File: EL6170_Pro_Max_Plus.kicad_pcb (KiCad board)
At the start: 2 copper layers, 128 x 70 mm, 0 parts

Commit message: key
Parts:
- added C1: 0.1uF, SparkFun-Capacitor:C_0603_1608Metric, F.Cu at (360.9, 159.2)
- added C10: 1uF, SparkFun-Capacitor:C_0402_1005Metric, F.Cu at (380.4, 162.9)
- added C11: 10uF, SparkFun-Capacitor:C_0402_1005Metric, F.Cu at (380.4, 164.8)
- added C12: 0.1uF, SparkFun-Capacitor:C_0402_1005Metric, F.Cu at (380.4, 166.8)
- added C13: 0.1uF, SparkFun-Capacitor:C_0402_1005Metric, F.Cu at (380.4, 168.8)
- added C14: 0.1uF, SparkFun-Capacitor:C_0402_1005Metric, F.Cu at (380.4, 170.7)
- added C15: 0.1uF, SparkFun-Capacitor:C_0402_1005Metric, F.Cu at (383.2, 158.9)
- added C16: 10uF, SparkFun-Capacitor:C_0402_1005Metric, F.Cu at (383.2, 160.9)
- added C17: 0.1uF, SparkFun-Capacitor:C_0402_1005Metric, F.Cu at (383.2, 162.9)
- added C18: 10uF, SparkFun-Capacitor:C_0402_1005Metric, F.Cu at (383.2, 164.8)
- added C19: 0.1uF, SparkFun-Capacitor:C_0402_1005Metric, F.Cu at (383.2, 166.8)
- added C2: 4.7uF, SparkFun-Capacitor:C_0603_1608Metric, F.Cu at (360.9, 161.7)
- added C20: 1uF, SparkFun-Capacitor:C_0402_1005Metric, F.Cu at (383.2, 168.8)
- added C21: 0.1uF, SparkFun-Capacitor:C_0402_1005Metric, F.Cu at (383.2, 170.7)
- added C22: 10pF, SparkFun-Capacitor:C_0603_1608Metric, F.Cu at (360.9, 176.8)
- added C23: 10pF, SparkFun-Capacitor:C_0603_1608Metric, F.Cu at (360.9, 179.3)
- added C24: 10uF, SparkFun-Capacitor:C_0402_1005Metric, F.Cu at (386.1, 158.9)
- added C25: 0.1uF, SparkFun-Capacitor:C_0402_1005Metric, F.Cu at (386.1, 160.9)
- added C26: 4.7pF, SparkFun-Capacitor:C_0402_1005Metric, F.Cu at (386.1, 162.9)
- added C27: 2.2nF, SparkFun-Capacitor:C_0603_1608Metric, F.Cu at (364.9, 159.2)
- added C28: 2.2nF, SparkFun-Capacitor:C_0603_1608Metric, F.Cu at (364.9, 161.7)
- added C29: 2.2uF, SparkFun-Capacitor:C_0603_1608Metric, F.Cu at (364.9, 164.2)
- added C3: 0.1uF, SparkFun-Capacitor:C_0603_1608Metric, F.Cu at (360.9, 164.2)
- added C30: 2.2uF, SparkFun-Capacitor:C_0603_1608Metric, F.Cu at (364.9, 166.7)
- added C31: 0.1uF, SparkFun-Capacitor:C_0603_1608Metric, F.Cu at (364.9, 169.2)
- added C32: 0.1uF, SparkFun-Capacitor:C_0603_1608Metric, F.Cu at (364.9, 171.7)
- added C33: 0.1uF, SparkFun-Capacitor:C_0603_1608Metric, F.Cu at (364.9, 174.3)
- added C34: 0.1uF, SparkFun-Capacitor:C_0603_1608Metric, F.Cu at (364.9, 176.8)
- added C35: 10uF, SparkFun-Capacitor:C_0603_1608Metric, F.Cu at (364.9, 179.3)
- added C36: 1uF, SparkFun-Capacitor:C_0603_1608Metric, F.Cu at (368.9, 159.2)
- added C37: 1uF, SparkFun-Capacitor:C_0603_1608Metric, F.Cu at (368.9, 161.7)
- added C38: 0.1uF, SparkFun-Capacitor:C_0603_1608Metric, F.Cu at (368.9, 164.2)
- added C39: 47uF, SparkFun-Capacitor:C_0805_2012Metric, F.Cu at (388.9, 153.3)
- added C4: 4.7uF, SparkFun-Capacitor:C_0603_1608Metric, F.Cu at (360.9, 166.7)
- added C40: 22uF, SparkFun-Capacitor:C_0603_1608Metric, F.Cu at (368.9, 166.7)
- added C41: 22uF, SparkFun-Capacitor:C_0603_1608Metric, F.Cu at (368.9, 169.2)
- added C42: 0.1uF, SparkFun-Capacitor:C_0603_1608Metric, F.Cu at (368.9, 171.7)
- added C43: 10uF, SparkFun-Capacitor:C_0603_1608Metric, F.Cu at (368.9, 174.3)
- added C44: 10uF, SparkFun-Capacitor:C_0402_1005Metric, F.Cu at (386.1, 164.8)
- added C45: 0.1uF, SparkFun-Capacitor:C_0402_1005Metric, F.Cu at (386.1, 166.8)
- added C5: 4.7uF, SparkFun-Capacitor:C_0603_1608Metric, F.Cu at (360.9, 169.2)
- added C6: 4.7uF, SparkFun-Capacitor:C_0603_1608Metric, F.Cu at (360.9, 171.7)
- added C7: 4.7uF, SparkFun-Capacitor:C_0603_1608Metric, F.Cu at (360.9, 174.3)
- added C8: 8.2pF, Capacitor_SMD:C_0402_1005Metric, F.Cu at (380.4, 158.9)
- added C9: 0.1uF, SparkFun-Capacitor:C_0402_1005Metric, F.Cu at (380.4, 160.9)
- added CN1: PJ-327A0-SMT, easyeda2kicad:AUDIO-SMD_PJ-327A0-SMT, F.Cu at (385.8, 138.5)
- added D1: LED, SparkFun-LED:LED_0603_1608Metric, F.Cu at (368.9, 176.8)
- added D10: LESD8D3.3CAT5G, Diode_SMD:D_SOD-882, F.Cu at (394.6, 191.1)
- added D11: LESD8D3.3CAT5G, Diode_SMD:D_SOD-882, F.Cu at (394.6, 193.4)
- added D12: 1N4148WS, Diode_SMD:D_SOD-323, F.Cu at (308.1, 159.4)
- added D13: 1N4148WS, Diode_SMD:D_SOD-323, F.Cu at (308.1, 162.4)
- added D14: 1N4148WS, Diode_SMD:D_SOD-323, F.Cu at (308.1, 165.3)
- added D15: 1N4148WS, Diode_SMD:D_SOD-323, F.Cu at (308.1, 168.3)
- added D16: 1N4148WS, Diode_SMD:D_SOD-323, F.Cu at (308.1, 171.2)
- added D17: 1N4148WS, Diode_SMD:D_SOD-323, F.Cu at (308.1, 174.2)
- added D18: 1N4148WS, Diode_SMD:D_SOD-323, F.Cu at (308.1, 177.1)
- added D19: 1N4148WS, Diode_SMD:D_SOD-323, F.Cu at (308.1, 180.1)
- added D2: LED, SparkFun-LED:LED_0603_1608Metric, F.Cu at (368.9, 179.3)
- added D20: 1N4148WS, Diode_SMD:D_SOD-323, F.Cu at (308.1, 183.0)
- added D21: 1N4148WS, Diode_SMD:D_SOD-323, F.Cu at (312.4, 159.4)
- added D22: 1N4148WS, Diode_SMD:D_SOD-323, F.Cu at (312.4, 162.4)
- added D23: 1N4148WS, Diode_SMD:D_SOD-323, F.Cu at (312.4, 165.3)
- added D24: 1N4148WS, Diode_SMD:D_SOD-323, F.Cu at (312.4, 168.3)
- added D25: 1N4148WS, Diode_SMD:D_SOD-323, F.Cu at (312.4, 171.2)
- added D26: 1N4148WS, Diode_SMD:D_SOD-323, F.Cu at (312.4, 174.2)
- added D27: 1N4148WS, Diode_SMD:D_SOD-323, F.Cu at (312.4, 177.1)
- added D28: 1N4148WS, Diode_SMD:D_SOD-323, F.Cu at (312.4, 180.1)
- added D29: 1N4148WS, Diode_SMD:D_SOD-323, F.Cu at (312.4, 183.0)
- added D3: SS14, Diode_SMD:D_SMA, F.Cu at (324.4, 193.3)
- added D30: 1N4148WS, Diode_SMD:D_SOD-323, F.Cu at (316.7, 159.4)
- added D31: 1N4148WS, Diode_SMD:D_SOD-323, F.Cu at (316.7, 162.4)
- added D32: 1N4148WS, Diode_SMD:D_SOD-323, F.Cu at (316.7, 165.3)
- added D33: 1N4148WS, Diode_SMD:D_SOD-323, F.Cu at (316.7, 168.3)
- added D34: 1N4148WS, Diode_SMD:D_SOD-323, F.Cu at (316.7, 171.2)
- added D35: 1N4148WS, Diode_SMD:D_SOD-323, F.Cu at (316.7, 174.2)
- added D36: 1N4148WS, Diode_SMD:D_SOD-323, F.Cu at (316.7, 177.1)
- added D37: 1N4148WS, Diode_SMD:D_SOD-323, F.Cu at (316.7, 180.1)
- added D38: 1N4148WS, Diode_SMD:D_SOD-323, F.Cu at (316.7, 183.0)
- added D39: 1N4148WS, Diode_SMD:D_SOD-323, F.Cu at (321.0, 159.4)
- added D4: LED, SparkFun-LED:LED_0603_1608Metric, F.Cu at (372.9, 159.2)
- added D40: 1N4148WS, Diode_SMD:D_SOD-323, F.Cu at (321.0, 162.4)
- added D41: 1N4148WS, Diode_SMD:D_SOD-323, F.Cu at (321.0, 165.3)
- added D42: 1N4148WS, Diode_SMD:D_SOD-323, F.Cu at (321.0, 168.3)
- added D43: 1N4148WS, Diode_SMD:D_SOD-323, F.Cu at (321.0, 171.2)
- added D44: 1N4148WS, Diode_SMD:D_SOD-323, F.Cu at (321.0, 174.2)
- added D45: 1N4148WS, Diode_SMD:D_SOD-323, F.Cu at (321.0, 177.1)
- added D46: 1N4148WS, Diode_SMD:D_SOD-323, F.Cu at (321.0, 180.1)
- added D47: 1N4148WS, Diode_SMD:D_SOD-323, F.Cu at (321.0, 183.0)
- added D48: 1N4148WS, Diode_SMD:D_SOD-323, F.Cu at (325.3, 159.4)
- added D49: 1N4148WS, Diode_SMD:D_SOD-323, F.Cu at (325.3, 162.4)
- added D5: SS34, Diode_SMD:D_SMA, F.Cu at (324.4, 197.9)
- added D50: 1N4148WS, Diode_SMD:D_SOD-323, F.Cu at (325.3, 165.3)
- added D51: 1N4148WS, Diode_SMD:D_SOD-323, F.Cu at (325.3, 168.3)
- added D52: 1N4148WS, Diode_SMD:D_SOD-323, F.Cu at (325.3, 171.2)
- added D53: 1N4148WS, Diode_SMD:D_SOD-323, F.Cu at (325.3, 174.2)
- added D54: 1N4148WS, Diode_SMD:D_SOD-323, F.Cu at (325.3, 177.1)
- added D55: 1N4148WS, Diode_SMD:D_SOD-323, F.Cu at (325.3, 180.1)
- added D56: 1N4148WS, Diode_SMD:D_SOD-323, F.Cu at (325.3, 183.0)
- added D57: 1N4148WS, Diode_SMD:D_SOD-323, F.Cu at (329.6, 159.4)
- added D58: 1N4148WS, Diode_SMD:D_SOD-323, F.Cu at (329.6, 162.4)
- added D59: 1N4148WS, Diode_SMD:D_SOD-323, F.Cu at (329.6, 165.3)
- added D6: LESD8D3.3CAT5G, Diode_SMD:D_SOD-882, F.Cu at (394.6, 181.7)
- added D60: 1N4148WS, Diode_SMD:D_SOD-323, F.Cu at (329.6, 168.3)
- added D61: 1N4148WS, Diode_SMD:D_SOD-323, F.Cu at (329.6, 171.2)
- added D62: 1N4148WS, Diode_SMD:D_SOD-323, F.Cu at (329.6, 174.2)
- added D63: 1N4148WS, Diode_SMD:D_SOD-323, F.Cu at (329.6, 177.1)
- added D64: 1N4148WS, Diode_SMD:D_SOD-323, F.Cu at (329.6, 180.1)
- added D7: LESD8D3.3CAT5G, Diode_SMD:D_SOD-882, F.Cu at (394.6, 184.0)
- added D8: LESD8D3.3CAT5G, Diode_SMD:D_SOD-882, F.Cu at (394.6, 186.4)
- added D9: LESD8D3.3CAT5G, Diode_SMD:D_SOD-882, F.Cu at (394.6, 188.7)
- added J1: USB_C_Receptacle, SparkFun-Connector:USB-C_16, F.Cu at (387.1, 122.0)
- added J2: microSD, SparkFun-Connector:microSD_External_Pin, F.Cu at (340.8, 170.0)
- added L1: 39nH, Inductor_SMD:L_0402_1005Metric, F.Cu at (383.1, 110.3)
- added L2: 1.3nH, Inductor_SMD:L_0402_1005Metric, F.Cu at (383.1, 112.3)
- added L3: 2nH, Inductor_SMD:L_0402_1005Metric, F.Cu at (383.1, 114.3)
- added L4: 2nH, Inductor_SMD:L_0402_1005Metric, F.Cu at (383.1, 116.3)
- added L5: 10uH_5x5mm_1.0A, SparkFun-Coil:Inductor_4.7x4.7mm, F.Cu at (390.9, 161.3)
- added L6: SCCD43-220KT, easyeda2kicad:IND-SMD_L4.5-W4.0_SCCD43, F.Cu at (390.9, 167.6)
- added Q1: MMBT3904, Package_TO_SOT_SMD:SOT-23, F.Cu at (379.2, 111.7)
- added Q2: MMBT3904, Package_TO_SOT_SMD:SOT-23, F.Cu at (379.2, 116.4)
- added Q3: 2N7002, Package_TO_SOT_SMD:SOT-23, F.Cu at (379.2, 121.0)
- added Q4: AO3401A, Package_TO_SOT_SMD:SOT-23, F.Cu at (379.2, 125.6)
- added Q5: AO3401A, Package_TO_SOT_SMD:SOT-23, F.Cu at (379.2, 130.2)
- added R1: 560, SparkFun-Resistor:R_0402_1005Metric, F.Cu at (383.1, 118.3)
- added R10: 15k, SparkFun-Resistor:R_0603_1608Metric, F.Cu at (372.9, 161.7)
- added R11: 205K, SparkFun-Resistor:R_0603_1608Metric, F.Cu at (372.9, 164.2)
- added R12: 1.8M, SparkFun-Resistor:R_0603_1608Metric, F.Cu at (372.9, 166.7)
- added R13: 470, SparkFun-Resistor:R_0603_1608Metric, F.Cu at (372.9, 169.2)
- added R14: 470, SparkFun-Resistor:R_0603_1608Metric, F.Cu at (372.9, 171.7)
- added R15: 470, SparkFun-Resistor:R_0603_1608Metric, F.Cu at (372.9, 174.3)
- added R16: 470, SparkFun-Resistor:R_0603_1608Metric, F.Cu at (372.9, 176.8)
- added R17: 470, SparkFun-Resistor:R_0603_1608Metric, F.Cu at (372.9, 179.3)
- added R18: 470, SparkFun-Resistor:R_0603_1608Metric, F.Cu at (376.9, 159.2)
- added R19: 0, SparkFun-Resistor:R_0603_1608Metric, F.Cu at (376.9, 161.7)
- added R2: 5.1k, SparkFun-Resistor:R_0402_1005Metric, F.Cu at (383.1, 120.3)
- added R20: 1k, SparkFun-Resistor:R_0603_1608Metric, F.Cu at (376.9, 164.2)
- added R21: 330, SparkFun-Resistor:R_0603_1608Metric, F.Cu at (376.9, 166.7)
- added R22: 330, SparkFun-Resistor:R_0603_1608Metric, F.Cu at (376.9, 169.2)
- added R23: 2, SparkFun-Resistor:R_0603_1608Metric, F.Cu at (376.9, 171.7)
- added R24: 10k, SparkFun-Resistor:R_0402_1005Metric, F.Cu at (388.9, 112.3)
- added R25: 10k, SparkFun-Resistor:R_0402_1005Metric, F.Cu at (388.9, 114.3)
- added R26: 10k, SparkFun-Resistor:R_0402_1005Metric, F.Cu at (388.9, 116.3)
- added R27: 10k, SparkFun-Resistor:R_0402_1005Metric, F.Cu at (388.9, 118.3)
- added R28: 10k, SparkFun-Resistor:R_0402_1005Metric, F.Cu at (388.9, 120.3)
- added R29: 10k, SparkFun-Resistor:R_0402_1005Metric, F.Cu at (391.8, 110.3)
- added R3: 5.1k, SparkFun-Resistor:R_0402_1005Metric, F.Cu at (386.0, 110.3)
- added R30: 10k, SparkFun-Resistor:R_0402_1005Metric, F.Cu at (391.8, 112.3)
- added R31: 10k, SparkFun-Resistor:R_0402_1005Metric, F.Cu at (391.8, 114.3)
- added R32: 10k, SparkFun-Resistor:R_0402_1005Metric, F.Cu at (391.8, 116.3)
- added R33: 10k, SparkFun-Resistor:R_0402_1005Metric, F.Cu at (391.8, 118.3)
- added R4: 4.7k, SparkFun-Resistor:R_0402_1005Metric, F.Cu at (386.0, 112.3)
- added R5: 4.7k, SparkFun-Resistor:R_0402_1005Metric, F.Cu at (386.0, 114.3)
- added R6: 4.7k, SparkFun-Resistor:R_0402_1005Metric, F.Cu at (386.0, 116.3)
- added R7: 499, SparkFun-Resistor:R_0402_1005Metric, F.Cu at (386.0, 118.3)
- added R8: 4.7k, SparkFun-Resistor:R_0402_1005Metric, F.Cu at (386.0, 120.3)
- added R9: 4.7k, SparkFun-Resistor:R_0402_1005Metric, F.Cu at (388.9, 110.3)
- added SH1: ~, SH1122:SH1122_FPC, F.Cu at (386.1, 151.1)
- added SW1: SW_LEFT, Butm:MaskBtm6mmBh, B.Cu at (147.5, 76.5)
- added SW10: SW_K4, Butm:MaskBtm4mmBh, B.Cu at (175.0, 90.5)
- added SW11: SW_K5, Butm:MaskBtm4mmBh, B.Cu at (162.5, 90.5)
- added SW12: SW_K6, Butm:MaskBtm4mmBh, B.Cu at (150.0, 90.5)
- added SW13: SW_K7, Butm:MaskBtm4mmBh, B.Cu at (137.5, 90.5)
- added SW14: SW_K8, Butm:MaskBtm4mmBh, B.Cu at (125.0, 90.5)
- added SW15: SW_K9, Butm:MaskBtm4mmBh, B.Cu at (112.5, 90.5)
- added SW16: SW_K0, Butm:MaskBtm4mmBh, B.Cu at (100.0, 90.5)
- added SW17: SW_KQ, Butm:MaskBtm5mm, B.Cu at (163.3, 146.1)
- added SW18: SW_KW, Butm:MaskBtm5mm, B.Cu at (163.3, 154.2)
- added SW19: SW_KE, Butm:MaskBtm5mm, B.Cu at (163.3, 162.3)
- added SW2: SW_UP, Butm:MaskBtm6mm, B.Cu at (136.5, 71.5)
- added SW20: SW_KR, Butm:MaskBtm5mm, B.Cu at (163.3, 170.4)
- added SW21: SW_KT, Butm:MaskBtm5mm, B.Cu at (163.3, 178.5)
- added SW22: SW_KY, Butm:MaskBtm5mm, B.Cu at (163.3, 186.6)
- added SW23: SW_KU, Butm:MaskBtm5mm, B.Cu at (155.2, 146.1)
- added SW24: SW_KI, Butm:MaskBtm5mm, B.Cu at (155.2, 154.2)
- added SW25: SW_KO, Butm:MaskBtm5mm, B.Cu at (155.2, 162.3)
- added SW26: SW_KP, Butm:MaskBtm5mm, B.Cu at (155.2, 170.4)
- added SW27: SW_KA, Butm:MaskBtm5mm, B.Cu at (155.2, 178.5)
- added SW28: SW_KS, Butm:MaskBtm5mm, B.Cu at (155.2, 186.6)
- added SW29: SW_KD, Butm:MaskBtm5mm, B.Cu at (147.1, 146.1)
- added SW3: SW_DOWN, Butm:MaskBtm6mm, B.Cu at (136.5, 81.0)
- added SW30: SW_KF, Butm:MaskBtm5mm, B.Cu at (147.1, 154.2)
- added SW31: SW_KG, Butm:MaskBtm5mm, B.Cu at (147.1, 162.3)
- added SW32: SW_KH, Butm:MaskBtm5mm, B.Cu at (147.1, 170.4)
- added SW33: SW_KJ, Butm:MaskBtm5mm, B.Cu at (147.1, 178.5)
- added SW34: SW_KK, Butm:MaskBtm5mm, B.Cu at (147.1, 186.6)
- added SW35: SW_KL, Butm:MaskBtm5mm, B.Cu at (139.0, 146.1)
- added SW36: SW_KZ, Butm:MaskBtm5mm, B.Cu at (139.0, 154.2)
- added SW37: SW_KX, Butm:MaskBtm5mm, B.Cu at (139.0, 162.3)
- added SW38: SW_KC, Butm:MaskBtm5mm, B.Cu at (139.0, 170.4)
- added SW39: SW_KV, Butm:MaskBtm5mm, B.Cu at (139.0, 178.5)
- added SW4: SW_RIGHT, Butm:MaskBtm6mmBh, B.Cu at (125.5, 76.5)
- added SW40: SW_KB, Butm:MaskBtm5mm, B.Cu at (139.0, 186.6)
- added SW41: SW_KN, Butm:MaskBtm5mm, B.Cu at (130.9, 146.1)
- added SW42: SW_KM, Butm:MaskBtm5mm, B.Cu at (130.9, 154.2)
- added SW43: SW_KCOM, Butm:MaskBtm5mm, B.Cu at (130.9, 162.3)
- added SW44: SW_KDOT, Butm:MaskBtm5mm, B.Cu at (130.9, 170.4)
- added SW45: SW_SHIFT, Butm:MaskBtm5mm, B.Cu at (130.9, 178.5)
- added SW46: SW_CE(IO0), Butm:MaskBtm5mm, B.Cu at (130.9, 186.6)
- added SW47: SW_OFF, Butm:MaskBtm5mm, B.Cu at (122.8, 146.1)
- added SW48: SW_SECRET, Butm:MaskBtm5mm, B.Cu at (122.8, 154.2)
- added SW49: SW_MCK, Butm:MaskBtm5mm, B.Cu at (122.8, 162.3)
- added SW5: SW_UP2, Butm:MaskBtm6mm, B.Cu at (113.0, 76.5)
- added SW50: SW_SPACE, Butm:MaskBtm5mmBh, B.Cu at (200.9, 170.3)
- added SW51: SW_REMARK, Butm:MaskBtm5mm, B.Cu at (122.8, 170.4)
- added SW52: SW_CALENDAR, Butm:MaskBtm5mm, B.Cu at (122.8, 178.5)
- added SW53: SW_MODE, Butm:MaskBtm5mm, B.Cu at (122.8, 186.6)
- added SW54: SW_ENTER, Butm:MaskBtm5mmBh, B.Cu at (199.0, 186.3)
- added SW6: SW_DOWN2, Butm:MaskBtm6mm, B.Cu at (100.5, 76.5)
- added SW7: SW_K1, Butm:MaskBtm4mmBh, B.Cu at (212.5, 90.5)
- added SW8: SW_K2, Butm:MaskBtm4mmBh, B.Cu at (200.0, 90.5)
- added SW9: SW_K3, Butm:MaskBtm4mmBh, B.Cu at (187.5, 90.5)
- added SWBOOT1: BOOT, Butm:MaskBtm4mm, F.Cu at (335.3, 190.5)
- added SWRST1: RST, Butm:MaskBtm4mm, F.Cu at (335.3, 197.6)
- added U1: ESP32-S3, Package_DFN_QFN:QFN-56-1EP_7x7mm_P0.4mm_EP4x4mm, F.Cu at (315.7, 189.1)
- added U10: ME6211C33M5, Package_TO_SOT_SMD:SOT-23-5, F.Cu at (308.5, 196.1)
- added U11: TP5400_C2891434, easyeda2kicad:ESOP-8_L4.9-W3.9-P1.27-LS6.0-BL-EP, F.Cu at (391.9, 175.7)
- added U12: PCF8575DBR, Package_SO:SSOP-24_5.3x8.2mm_P0.65mm, F.Cu at (344.1, 192.0)
- added U2: TPS61040DBV, Package_TO_SOT_SMD:SOT-23-5, F.Cu at (308.5, 186.9)
- added U3: ESP-PSRAM64H, Package_SO:SOIC-8_3.9x4.9mm_P1.27mm, F.Cu at (354.0, 197.7)
- added U4: W25Q128JVS, Package_SO:SOIC-8_5.23x5.23mm_P1.27mm, F.Cu at (359.7, 150.5)
- added U5: ME6217C33M5, Package_TO_SOT_SMD:SOT-23-5, F.Cu at (308.5, 191.5)
- added U6: CH340K, Package_SO:SSOP-10-1EP_3.9x4.9mm_P1mm_EP2.1x3.3mm, F.Cu at (315.4, 197.2)
- added U7: RFANT5220110A0T, easyeda2kicad:FILTER-SMD_L5.2-W2.0-L, F.Cu at (325.8, 187.8)
- added U8: CH334R, Package_SO:QSOP-16_3.9x4.9mm_P0.635mm, F.Cu at (369.5, 150.3)
- added U9: PCM5102A, Package_SO:TSSOP-20_4.4x6.5mm_P0.65mm, F.Cu at (383.7, 175.8)
- added X1: 40MHz, easyeda2kicad:CRYSTAL-SMD_4P-L2.5-W2.0-BL, F.Cu at (379.3, 153.9)
- added X2: 12MHz, easyeda2kicad:CRYSTAL-SMD_4P-L2.5-W2.0-BL-A, F.Cu at (384.3, 153.9)

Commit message: sync
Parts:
- moved C24 318.5 mm to (67.8, 145.7)
- moved C25 318.5 mm to (67.8, 147.6)
- moved C26 318.5 mm to (67.8, 149.6)
- moved C44 318.5 mm to (67.8, 151.6)
- moved C45 318.5 mm to (67.8, 153.5)
- moved D21 318.5 mm to (-5.84, 146.1)
- moved D22 318.5 mm to (-5.84, 149.1)
- moved D23 318.5 mm to (-5.84, 152.0)
- moved D24 318.5 mm to (-5.84, 155.0)
- moved D25 318.5 mm to (-5.84, 157.9)
- moved D26 318.5 mm to (-5.84, 160.9)
- moved D27 318.5 mm to (-5.84, 163.8)
- moved D28 318.5 mm to (-5.84, 166.8)
- moved D29 318.5 mm to (-5.84, 169.7)
- moved D30 318.5 mm to (-1.55, 146.1)
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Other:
- board size 128 x 70 mm -> 128 x 70.5 mm

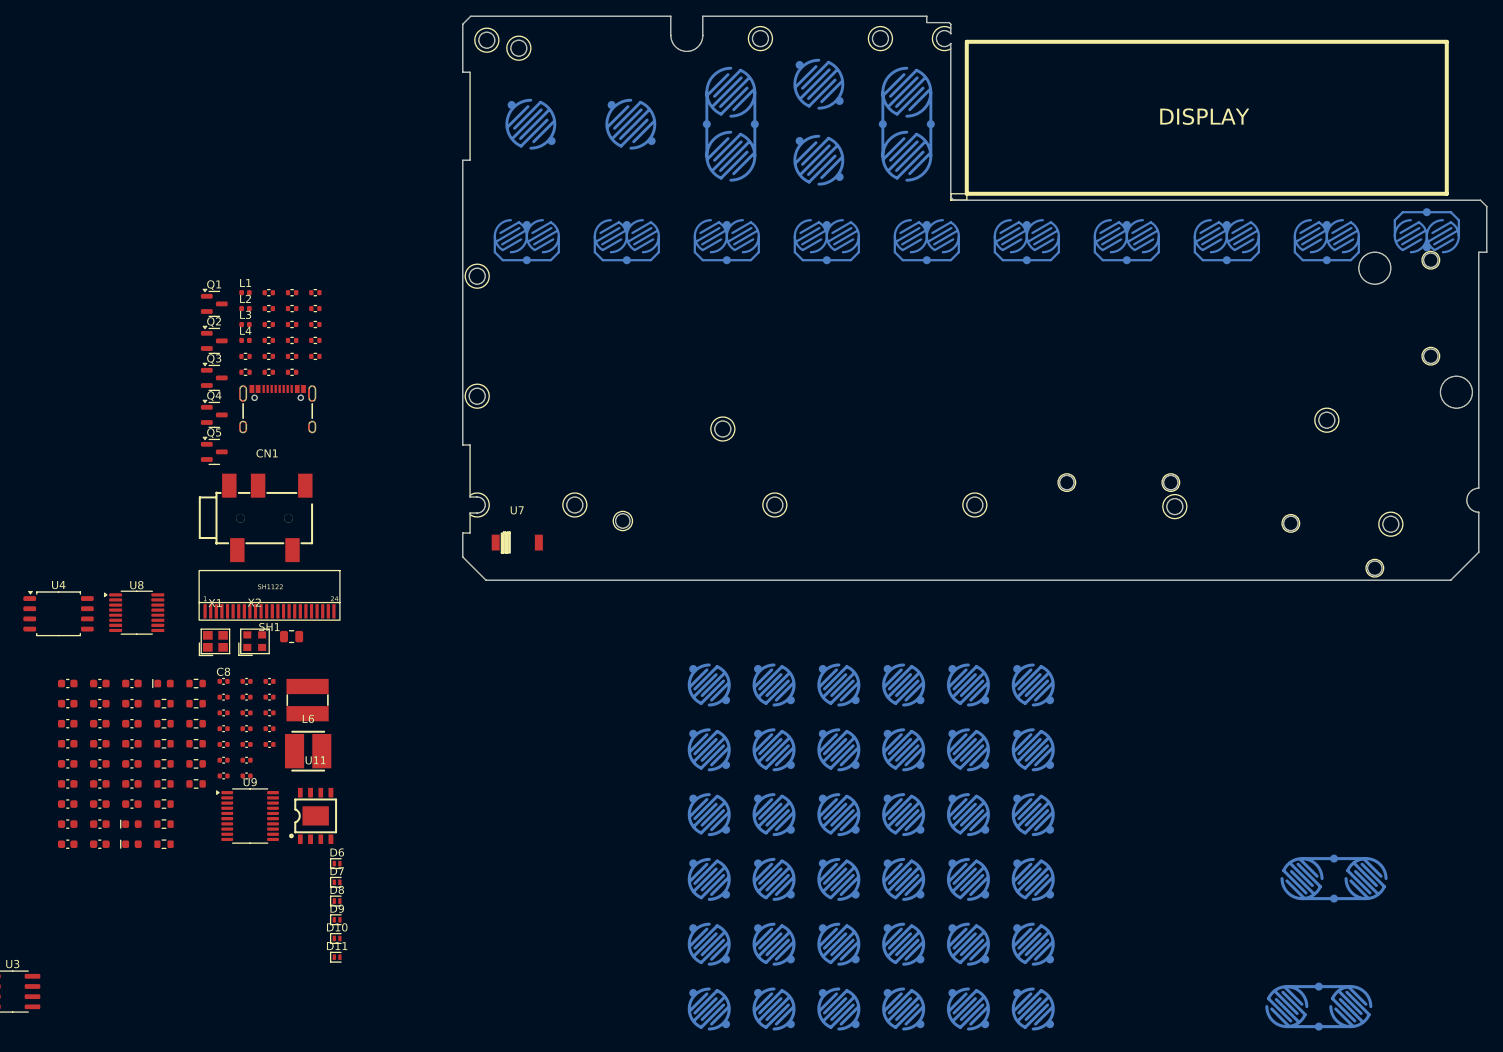
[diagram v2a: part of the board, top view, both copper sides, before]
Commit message: add some keypad
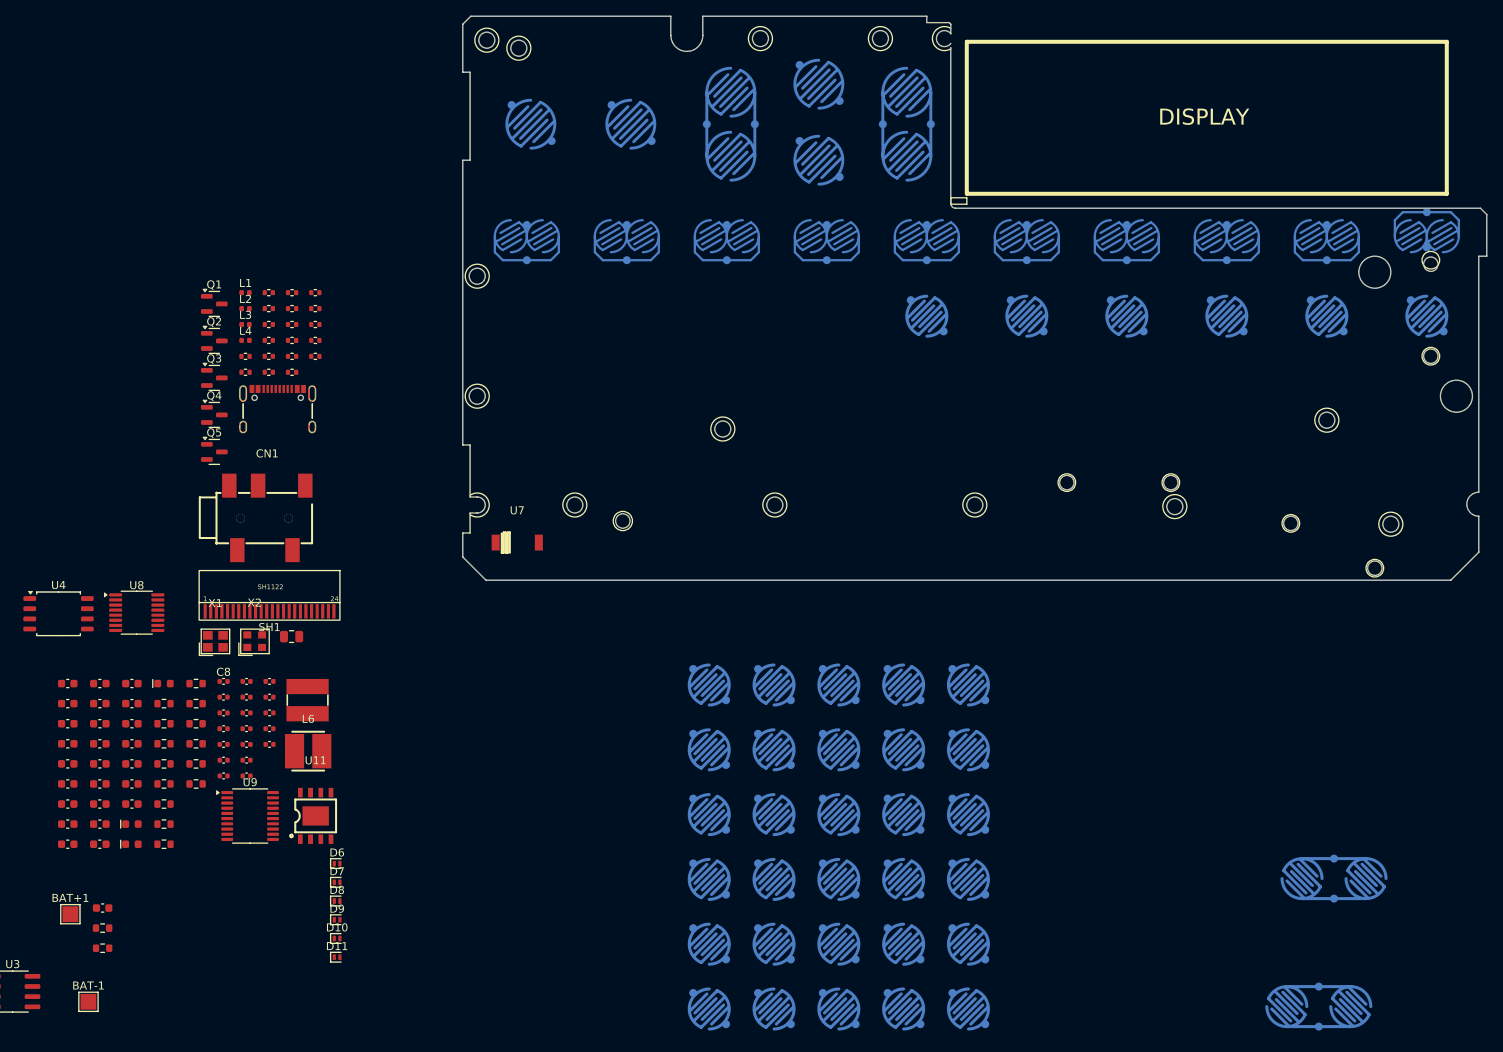
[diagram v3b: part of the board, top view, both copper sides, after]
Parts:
- added BAT+1: ~, TestPoint:TestPoint_Pad_2.0x2.0mm, F.Cu at (42.9, 174.8)
- added BAT-1: ~, TestPoint:TestPoint_Pad_2.0x2.0mm, F.Cu at (45.2, 185.7)
- added C46: 0.1uF, SparkFun-Capacitor:C_0603_1608Metric, F.Cu at (47.0, 174.0)
- added R34: 1M, SparkFun-Resistor:R_0603_1608Metric, F.Cu at (47.0, 176.5)
- added R35: 1M, SparkFun-Resistor:R_0603_1608Metric, F.Cu at (47.0, 179.0)
- moved SW22 87.6 mm to (150.0, 100.0)
- moved SW21 78.5 mm to (162.5, 100.0)
- moved SW20 71.4 mm to (175.0, 100.0)
- moved SW17 67.4 mm to (212.5, 100.0)
- moved SW19 66.8 mm to (187.5, 100.0)
- moved SW18 65.5 mm to (200.0, 100.0)
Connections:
- C40 pad 1: /VBAT -> DEMP
- C41 pad 1: /VBAT -> DEMP
- C42 pad 1: /VBAT -> DEMP
- L6 pad 2: /VBAT -> DEMP
- U1 pad 15: CARD_DET -> BAT_SMP
- U1 pad 24: GPIO18 -> CARD_DET
- U11 pad 6: /VBAT -> DEMP
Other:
- outline, holes or cut-outs redrawn

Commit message: sync
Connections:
- BAT+1 pad 1: DEMP -> /VBAT
- C40 pad 1: DEMP -> /VBAT
- C41 pad 1: DEMP -> /VBAT
- C42 pad 1: DEMP -> /VBAT
- L6 pad 2: DEMP -> /VBAT
- R34 pad 2: DEMP -> /VBAT
- U11 pad 6: DEMP -> /VBAT

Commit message: PCB layout
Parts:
- moved D18 230.1 mm to (208.3, 91.4)
- moved D28 224.6 mm to (208.0, 98.0)
- moved D19 224.2 mm to (201.1, 91.4), turned to 180 degrees
- moved D5 220.4 mm to (216.1, 117.5), turned to 90 degrees
- moved D29 219.5 mm to (201.6, 98.0), turned to 180 degrees
- moved D38 211.8 mm to (200.9, 107.5)
- moved D20 210.3 mm to (186.4, 95.0)
- moved U6 206.7 mm to (186.3, 100.7)
- moved D33 205.1 mm to (193.6, 92.0), turned to 180 degrees
- moved D55 201.2 mm to (204.2, 126.9)
- moved D30 200.9 mm to (193.5, 98.0), turned to 180 degrees
- moved D40 195.3 mm to (193.6, 107.5)
- moved D31 193.4 mm to (182.6, 90.0), turned to 180 degrees
- moved U5 190.7 mm to (172.1, 120.7)
- moved D54 189.1 mm to (192.4, 126.6)
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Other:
- outline, holes or cut-outs redrawn

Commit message: sync
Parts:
- moved R32 4.87 mm to (163.0, 104.6), turned to 45 degrees
- moved R25 1.40 mm to (171.9, 103.7)
- moved D2 1.30 mm to (158.2, 104.3), turned to 45 degrees
- moved L4 1.08 mm to (157.8, 108.3), turned to 45 degrees
- moved U1 1.00 mm to (165.9, 110.0), turned to 45 degrees
- moved R7 0.60 mm to (174.2, 105.4)
- moved R10 0.30 mm to (173.3, 109.9)
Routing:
- net SPIWP: track 0.00 -> 27.7 mm
- net /VDD_SPI: track 0.00 -> 24.2 mm, vias 0 -> 2
- net SPICS0: track 0.00 -> 20.6 mm
- net SPIQ: track 0.00 -> 16.8 mm
- net SPIHD: track 0.00 -> 12.6 mm, vias 0 -> 2
- net SPICLK: track 0.00 -> 10.1 mm
- net GPIO48: track 0.00 -> 7.35 mm, vias 0 -> 2
- net SPID: track 0.00 -> 6.91 mm
- net +3V3: track 0.00 -> 2.48 mm
- net GPIO39: track 0.00 -> 2.45 mm
- added copper zone on B.Cu, net DEMP
- added copper zone on F.Cu, net DEMP

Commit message: sync
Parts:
- added R36: 10k, SparkFun-Resistor:R_0402_1005Metric, F.Cu at (215.0, 123.3)
- moved C6 48.0 mm to (136.1, 85.8), turned to 0 degrees
- moved R32 7.02 mm to (156.7, 101.5), turned to 0 degrees
- moved C46 3.81 mm to (172.2, 117.6)
- moved R21 2.55 mm to (160.0, 124.0), turned to 180 degrees
- moved U12 1.82 mm to (182.6, 109.2)
- moved C36 1.80 mm to (142.0, 122.0)
- moved D42 1.39 mm to (164.1, 120.3)
- moved R26 0.64 mm to (149.0, 107.0), turned to 0 degrees
- moved R31 0.57 mm to (149.0, 108.3), turned to 0 degrees
- moved R30 0.40 mm to (149.0, 109.8), turned to 0 degrees
- moved R28 0.30 mm to (149.4, 103.5), turned to 0 degrees
- turned R24 to 0 degrees
- turned R27 to 0 degrees
- turned R29 to 0 degrees
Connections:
- U11 pad 4: STDBY -> GPIO2
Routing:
- net +3V3: track 2.48 -> 369.5 mm, vias 0 -> 25
- net +5V: track 0.00 -> 195.8 mm, vias 0 -> 6
- net /BAT5V: track 0.00 -> 99.9 mm, vias 0 -> 9
- net XSMT: track 0.00 -> 86.4 mm, vias 0 -> 2
- net /USB5V: track 0.00 -> 86.2 mm
- net CHIP_PU: track 0.00 -> 77.0 mm, vias 0 -> 3
- net GPIO17: track 0.00 -> 70.0 mm, vias 0 -> 2
- net GPIO14: track 0.00 -> 68.3 mm, vias 0 -> 2
- net AGND: track 0.00 -> 67.1 mm, vias 0 -> 2
- net GPIO13: track 0.00 -> 67.0 mm, vias 0 -> 2
- net GPIO12: track 0.00 -> 65.6 mm, vias 0 -> 2
- net GPIO11: track 0.00 -> 64.6 mm, vias 0 -> 2
- net GPIO0: track 0.00 -> 64.2 mm, vias 0 -> 3
- net CARD_DET: track 0.00 -> 63.3 mm
- net GPIO2: track 0.00 -> 62.3 mm, vias 0 -> 2
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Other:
- copper layers 2 -> 4

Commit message: sync
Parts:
- moved R10 0.30 mm to (173.6, 109.9)
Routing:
- net KEY_COL1: track 0.00 -> 243.8 mm, vias 0 -> 7
- net KEY_COL2: track 0.00 -> 240.2 mm, vias 0 -> 5
- net KEY_COL0: track 0.00 -> 220.7 mm, vias 0 -> 1
- net KEY_COL4: track 0.00 -> 205.7 mm, vias 0 -> 8
- net KEY_COL3: track 0.00 -> 203.0 mm, vias 0 -> 8
- net KEY_COL5: track 0.00 -> 154.6 mm, vias 0 -> 8
- net Net-(D2-K): track 0.00 -> 24.3 mm, vias 0 -> 2
- net XSMT: track 86.4 -> 100.0 mm
- net GPIO48: track 0.00 -> 11.9 mm, vias 0 -> 3
